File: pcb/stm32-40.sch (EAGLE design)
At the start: 103 parts, among them IC1 STM32F103RBT6, IC2 CAT24M01WI-GT3, IC3 MAX487-S, IC4 AMIS30663CANG2G, Q1 32768Hz, Q2 8MHz, Q3 MMBT2222, SW1 KSS-2EG4430, SW2 KSS-2EG4430, SW3 KSS-2EG4430, SW4 KSS-2EG4430, SW5 KSS-2EG4430, X1 MCV3, X2 MCV3

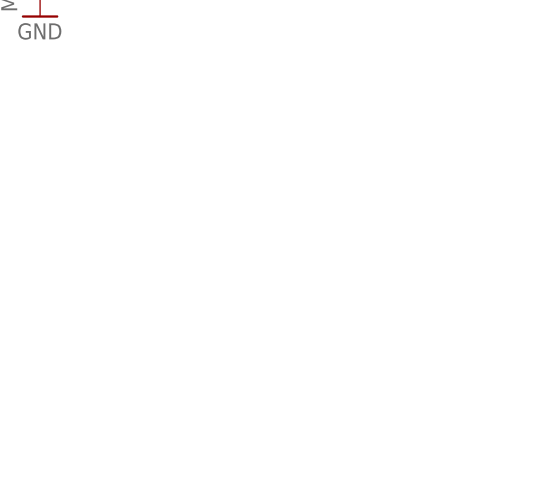
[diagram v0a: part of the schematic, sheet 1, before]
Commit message: stm32-40 ready to production PCB. some changes in platform
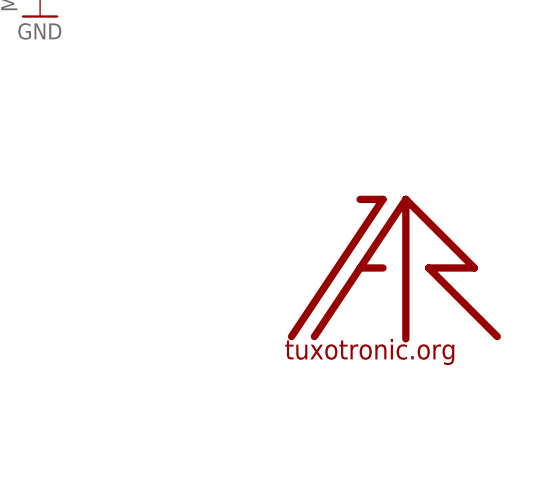
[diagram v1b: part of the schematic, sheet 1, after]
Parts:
- added U$1: LOGO, logo:LOGO
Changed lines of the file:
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@@
 <layer number="101" name="Patch_Top" color="12" fill="4" visible="yes" active="yes"/>
 <layer number="102" name="bot_pads" color="7" fill="5" visible="no" active="yes"/>
+<layer number="103" name="REF" color="7" fill="1" visible="yes" active="yes"/>
 <layer number="104" name="S_DOKU" color="7" fill="1" visible="no" active="yes"/>
 <layer number="105" name="Beschreib" color="9" fill="1" visible="no" active="no"/>
@@
 <layer number="107" name="BD-Top" color="5" fill="1" visible="no" active="no"/>
 <layer number="116" name="Patch_BOT" color="9" fill="4" visible="yes" active="yes"/>
+<layer number="121" name="_tsilk" color="7" fill="1" visible="no" active="yes"/>
+<layer number="122" name="_bsilk" color="7" fill="1" visible="no" active="yes"/>
+<layer number="125" name="_tNames" color="7" fill="1" visible="no" active="yes"/>
+<layer number="144" name="Drill_legend" color="7" fill="1" visible="no" active="yes"/>
 <layer number="151" name="HeatSink" color="7" fill="1" visible="no" active="yes"/>
 <layer number="199" name="Contour" color="7" fill="1" visible="no" active="yes"/>
 <layer number="200" name="200bmp" color="1" fill="10" visible="no" active="no"/>
 <layer number="201" name="201bmp" color="2" fill="1" visible="no" active="no"/>
+<layer number="202" name="202bmp" color="7" fill="1" visible="yes" active="yes"/>
+<layer number="203" name="203bmp" color="4" fill="10" visible="no" active="yes"/>
+<layer number="204" name="204bmp" color="5" fill="10" visible="no" active="yes"/>
+<layer number="205" name="205bmp" color="6" fill="10" visible="no" active="yes"/>
+<layer number="206" name="206bmp" color="7" fill="10" visible="no" active="yes"/>
+<layer number="207" name="207bmp" color="8" fill="10" visible="no" active="yes"/>
+<layer number="208" name="208bmp" color="9" fill="10" visible="no" active="yes"/>
+<layer number="209" name="209bmp" color="7" fill="1" visible="no" active="yes"/>
+<layer number="210" name="210bmp" color="7" fill="1" visible="no" active="yes"/>
+<layer number="211" name="211bmp" color="7" fill="1" visible="no" active="yes"/>
+<layer number="212" name="212bmp" color="7" fill="1" visible="no" active="yes"/>
+<layer number="213" name="213bmp" color="7" fill="1" visible="no" active="yes"/>
+<layer number="214" name="214bmp" color="7" fill="1" visible="no" active="yes"/>
+<layer number="215" name="215bmp" color="7" fill="1" visible="no" active="yes"/>
+<layer number="216" name="216bmp" color="7" fill="1" visible="no" active="yes"/>
+<layer number="217" name="217bmp" color="18" fill="1" visible="no" active="no"/>
+<layer number="218" name="218bmp" color="19" fill="1" visible="no" active="no"/>
+<layer number="219" name="219bmp" color="20" fill="1" visible="no" active="no"/>
+<layer number="220" name="220bmp" color="21" fill="1" visible="no" active="no"/>
+<layer number="221" name="221bmp" color="22" fill="1" visible="no" active="no"/>
+<layer number="222" name="222bmp" color="23" fill="1" visible="no" active="no"/>
+<layer number="223" name="223bmp" color="24" fill="1" visible="no" active="no"/>
+<layer number="224" name="224bmp" color="25" fill="1" visible="no" active="no"/>
 <layer number="231" name="Eagle3D_PG1" color="7" fill="1" visible="yes" active="yes"/>
 <layer number="232" name="Eagle3D_PG2" color="7" fill="1" visible="yes" active="yes"/>
@@
 <part name="L1" library="rc-master-smd" deviceset="FB_" device="0603" value="bead"/>
 <part name="+3V2" library="supply1" deviceset="+3V3" device=""/>
-<part name="FRAME1" library="frames-tt.org" deviceset="A3L-LOC" device=""/>
+<part name="FRAME1" library="frames-tt.org" deviceset="A3L-LOC" device="" value="MCU"/>
 <part name="IC2" library="stm32-by-pb" deviceset="AT24C*" device="S" technology="256" value="CAT24M01WI-GT3"/>
 <part name="C12" library="rc-master-smd" deviceset="C_" device="0603" value="0.1"/>
@@
 <part name="R9" library="rc-master-smd" deviceset="R_" device="0603" value="10K"/>
 <part name="R10" library="rc-master-smd" deviceset="R_" device="0603" value="10K"/>
-<part name="FRAME2" library="frames-tt.org" deviceset="A3L-LOC" device=""/>
+<part name="FRAME2" library="frames-tt.org" deviceset="A3L-LOC" device="" value="Connections"/>
 <part name="IC4" library="interfaces" deviceset="SN65HVD230" device="" value="AMIS30663CANG2G"/>
 <part name="+3V19" library="supply1" deviceset="+3V3" device=""/>
@@
 <part name="R50" library="rc-master-smd" deviceset="R_" device="0603" value="1K"/>
 <part name="GND13" library="supply1" deviceset="GND" device=""/>
+<part name="U$1" library="logo" deviceset="LOGO" device=""/>
 </parts>
 <sheets>
@@
 <instance part="R50" gate="G$1" x="177.8" y="38.1" rot="R90"/>
 <instance part="GND13" gate="1" x="177.8" y="30.48"/>
+<instance part="U$1" gate="G$1" x="355.6" y="25.4"/>
 </instances>
 <busses>

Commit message: little button fix
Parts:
- added R51: 330, rc-master-smd:R_0603
- C1, C2: value 10pF -> 0.1
- C14, C16: value 100uF/6V3 -> 0.1; device rc-master-smd:CP_SMCD -> rc-master-smd:C_0603
- C17: device rc-master-smd:C_0805 -> rc-master-smd:C_0603
- C19, C20: value 0.1 -> 560pF
- C21: value 0.1 -> 100uF/6V3; device rc-master-smd:C_0603 -> rc-master-smd:CP_SMCD
- C22: value 560pF -> 0.1; device rc-master-smd:C_0603 -> rc-master-smd:C_0805
- C23: value 560pF -> 100uF/6V3; device rc-master-smd:C_0603 -> rc-master-smd:CP_SMCD
- C3: value 22pF -> 0.1
- C4: value 22pF -> 10pF
- C5: value 0.1 -> 10pF
- C6, C7: value 0.1 -> 22pF
- IC1: value STM32F103RBT6 -> CAT24M01WI-GT3; device stm32:STM32F103R -> stm32-by-pb:AT24C256S
- IC2: value CAT24M01WI-GT3 -> STM32F103RBT6; device stm32-by-pb:AT24C256S -> stm32:STM32F103R
- IC3: value MAX487-S -> AMIS30663CANG2G; device rs232-rs485:MAX487-S -> interfaces:SN65HVD230
- IC4: value AMIS30663CANG2G -> MAX487-S; device interfaces:SN65HVD230 -> rs232-rs485:MAX487-S
- R1, R2: value 220 -> 10K
- R10: value 10K -> 2.2K
- R11, R41: value 4.7K -> 10K
- R12: value 4.7K -> 1K
- R13, R22: value 10 -> 2K
- R14: value 10 -> 3.9K
- R15: value 10 -> 1M
- R16: value 10 -> 1K
- R17, R18, R19: value 10 -> 200
- R20: value 10 -> 4.7K
- R23: value 10 -> 10K
- R24: value 10 -> 100
- R25, R27: value 560 -> 10
- R26: value 10K -> 10
- R28, R30: value 120 -> 10; device rc-master-smd:R_0805 -> rc-master-smd:R_0603
- R29, R31: value 330 -> 10
- R3, R4: value 10K -> 4.7K
- R32: value 0 -> 10
- R33, R34, R35: value 100 -> 10
- R36: value NC -> 10
- R42: value 200 -> 0
- R43: value 10 -> NC
- R44: value 2K -> 560
- R45: value 200 -> 100
- R46: value 200 -> 560
- R47: value 1K -> 100
- R48: value 2K -> 120; device rc-master-smd:R_0603 -> rc-master-smd:R_0805
- R49: value 3.9K -> 120; device rc-master-smd:R_0603 -> rc-master-smd:R_0805
- R5: value 10K -> 220
- R50: value 1K -> 330
- R6: value 2.2K -> 220
- R7: value 1M -> 10K
- renumbered JP2 to JP1, STMP40 to STMP1
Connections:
- new net PB5: IC2.PB5/I2C1_SMBA/(TIM3_CH2/SPI1_MOSI), R7.1
- net !LCD_CS: now also R19.2, R20.1; no longer R41.1, R46.2
- net !RESET: now also C3.1, IC2.!RESET, R11.1, SW1.S; no longer C5.1, IC1.!RESET, R8.1, SW2.S
- net +3V3: now also C1.1, C17.1, C2.1, C22.1, C23.+, IC1.VCC, IC2.VDD@1, IC2.VDD@2, IC2.VDD@3, IC2.VDD@4, R1.2, R2.2, R20.2, R21.2, R23.2, R3.2, R4.2, R42.1, R5.1, SW2.S; no longer C11.1, C15.1, C16.+, C20.1, C7.1, IC1.VDD@1, IC1.VDD@2, IC1.VDD@3, IC1.VDD@4, IC2.VCC, R1.1, R10.2, R12.2, R32.1, R41.2, R43.2, R5.2, R8.2, R9.2, SW1.S
- net +5V: now also C14.1, C15.1, C16.1, C21.+, IC3.VDD, IC4G$2.VCC, R46.2; no longer C14.+, C17.1, C18.1, C19.1, IC3G$2.VCC, IC4.VDD, R25.2
- net BOOT0: now also IC2.BOOT0, R8.1; no longer IC1.BOOT0, IC1.PB5/I2C1_SMBA/(TIM3_CH2/SPI1_MOSI), R4.1
- net BOOT1: now also IC2.PB2/BOOT1, R6.1, R9.1; no longer IC1.PB2/BOOT1, R2.1, R3.1
- net CAN_CTRL: now also IC3.RS, R42.2, R43.2; no longer IC4.RS, R32.2, R36.2
- net CAN_H: now also R49.1; no longer R30.1
- net CAN_RX: now also IC2.PA11/CANRX/USBDM/USART1_CTS/TIM1_CH4, R24.1; no longer IC1.PA11/CANRX/USBDM/USART1_CTS/TIM1_CH4, R33.1
- net CAN_TX: now also IC2.PA12/CANTX/USBDP/USART1_RTS/TIM1_ETR, IC3.TXD; no longer IC1.PA12/CANTX/USBDP/USART1_RTS/TIM1_ETR, IC4.TXD
- net DE3: now also IC2.PC12/(USART3_CK), IC4G$1.DI; no longer IC1.PC12/(USART3_CK), IC3G$1.DI
- net GND: now also C14.2, C16.2, C21.-, C23.-, IC1.A0, IC1.A1, IC1.A2, IC1.GND, IC1.WP, IC2.VSS@1, IC2.VSS@2, IC2.VSS@3, IC2.VSS@4, IC2.VSSA, IC3.VSS, IC4G$2.GND, R10.1, R16.1, R41.1, R43.1, R44.1, R9.2, SW1.P; no longer C14.-, C16.-, C21.2, C23.2, IC1.VSS@1, IC1.VSS@2, IC1.VSS@3, IC1.VSS@4, IC1.VSSA, IC2.A0, IC2.A1, IC2.A2, IC2.GND, IC2.WP, IC3G$2.GND, IC4.VSS, R26.1, R27.1, R3.2, R36.1, R50.1, R6.1, SW2.P
- net LCD_CLK: now also R18.2; no longer R45.2
- net LCD_DATA: now also R17.2; no longer R42.2
- net N$1: now also C18.1, IC3.VREF; no longer C21.1, IC4.VREF
- net N$10: now also R51.1; no longer R31.1
- net N$11: now also R33.1; no longer R21.1
- net N$13: now also R5.2; no longer R1.2
- net N$14: now also R34.1; no longer R22.1
- net N$15: now also R25.1; no longer R13.1
- net N$16: now also R26.1; no longer R14.1
- net N$17: now also R27.1; no longer R15.1
- net N$18: now also R28.1; no longer R16.1
- net N$19: now also R29.1; no longer R17.1
- net N$2: now also R49.2; no longer R30.2
- net N$20: now also R30.1; no longer R18.1
- net N$21: now also R31.1; no longer R19.1
- net N$22: now also R32.1; no longer R20.1
- net N$23: now also R35.1; no longer R23.1
- net N$24: now also R36.1; no longer R24.1
- net N$3: now also R10.2, R7.2, R8.2, SW2.P; no longer R4.2, R6.2, SW1.P
- net N$30: now also R6.2; no longer R2.2
- net N$31: now also R21.1; no longer R43.1
- net N$32: now also R22.1; no longer R44.1
- net N$33: now also R12.1; no longer R47.1
- net N$34: now also R13.1; no longer R48.1
- net N$35: now also R14.1; no longer R49.1
- net N$44: now also IC4G$1.A, R46.1; no longer IC3G$1.A, R25.1
- net N$51: now also IC3.CANH, R45.2; no longer IC4.CANH, R34.2
- net N$52: now also IC3.CANL, R47.2; no longer IC4.CANL, R35.2
- net N$54: now also C20.1, R47.1; no longer C23.1, R35.1
- net N$55: now also C19.1, R45.1; no longer C22.1, R34.1
- net N$6: now also IC4G$1.B, R44.2; no longer IC3G$1.B, R27.2
- net N$7: now also IC3.RXD, R24.2; no longer IC4.RXD, R33.2
- net N$8: now also R48.2; no longer R28.2
- net N$9: now also R50.1; no longer R29.1
- net OSC32_IN: now also C4.1, IC2.PC14/OSC32_IN; no longer C1.1, IC1.PC14/OSC32_IN
- net OSC32_OUT: now also C5.1, IC2.PC15/OSC32_OUT; no longer C2.1, IC1.PC15/OSC32_OUT
- net OSC_IN: now also C6.1, IC2.OSC_IN/(PD0/CANRX), R15.2; no longer C3.1, IC1.OSC_IN/(PD0/CANRX), R7.2
- net OSC_OUT: now also C7.1, IC2.OSC_OUT/(PD1/CANTX), R15.1; no longer C4.1, IC1.OSC_OUT/(PD1/CANTX), R7.1
- net PA0: now also IC2.PA0/WKUP/USART2_CTS/ADC12_IN0/TIM2_CH1_ETR, R12.2, R13.2, R14.2, R16.2; no longer IC1.PA0/WKUP/USART2_CTS/ADC12_IN0/TIM2_CH1_ETR, R47.2, R48.2, R49.2, R50.2
- net PA1: now also IC2.PA1/USART2_RTS/ADC12_IN1/TIM2_CH2, R19.1; no longer IC1.PA1/USART2_RTS/ADC12_IN1/TIM2_CH2, R46.1
- net PA15: now also IC2.JTDI/(TIM2_CH1_ETR/PA15/SPI1_NSS); no longer IC1.JTDI/(TIM2_CH1_ETR/PA15/SPI1_NSS)
- net PA2: now also IC2.PA2/USART2_TX/ADC12_IN2/TIM2_CH3, R17.1; no longer IC1.PA2/USART2_TX/ADC12_IN2/TIM2_CH3, R42.1
- net PA3: now also IC2.PA3/USART2_RX/ADC12_IN3/TIM2_CH4; no longer IC1.PA3/USART2_RX/ADC12_IN3/TIM2_CH4
- net PA4: now also IC2.PA4/SPI1_NSS/ADC12_IN4/USART2_CK, R18.1; no longer IC1.PA4/SPI1_NSS/ADC12_IN4/USART2_CK, R45.1
- net PA5: now also IC2.PA5/SPI1_SCK/ADC12_IN5; no longer IC1.PA5/SPI1_SCK/ADC12_IN5
- net PA6: now also IC2.PA6/SPI1_MISO/ADC12_IN6/TIM3_CH1; no longer IC1.PA6/SPI1_MISO/ADC12_IN6/TIM3_CH1
- net PA7: now also IC2.PA7SPI1_MOSI/ADC12_IN7/TIM3_CH2; no longer IC1.PA7SPI1_MOSI/ADC12_IN7/TIM3_CH2
- net PA8: now also IC2.PA8/USART1_CK/MCO/TIM1_CH1; no longer IC1.PA8/USART1_CK/MCO/TIM1_CH1
- net PB0: now also IC2.PB0/ADC12_IN8/TIM3_CH3/(TIM1_CH2N); no longer IC1.PB0/ADC12_IN8/TIM3_CH3/(TIM1_CH2N)
- net PB1: now also IC2.PB1/ADC12_IN9/TIM3_CH4/(TIM1_CH3N); no longer IC1.PB1/ADC12_IN9/TIM3_CH4/(TIM1_CH3N)
- net PC0: now also IC2.PC0/ADC10, R33.2; no longer IC1.PC0/ADC10, R21.2
- net PC1: now also IC2.PC1/ADC11, R34.2; no longer IC1.PC1/ADC11, R22.2
- net PC13: now also IC2.PC13/TAMPER-RTC; no longer IC1.PC13/TAMPER-RTC
- net PC2: now also IC2.PC2/ADC12, R35.2; no longer IC1.PC2/ADC12, R23.2
- net PC3: now also IC2.PC3/ADC13, R36.2; no longer IC1.PC3/ADC13, R24.2
- net PC4: now also IC2.PC4/ADC14; no longer IC1.PC4/ADC14
- net PC5: now also IC2.PC5/ADC15; no longer IC1.PC5/ADC15
- net PD2: now also IC2.PD2/TIM3_ETR, R22.2; no longer IC1.PD2/TIM3_ETR, R44.2
- net RS485_A: now also R48.1; no longer R28.1
- net RXD1: now also IC2.PA10/USART1_RX/TIM1_CH3, R23.1; no longer IC1.PA10/USART1_RX/TIM1_CH3, R5.1
- net RXD3: now also IC2.PC11/(USART3_RX), IC4G$1.RO; no longer IC1.PC11/(USART3_RX), IC3G$1.RO
- net SCL2: now also IC1.SCL, IC2.PB10/I2C2_SCL/USART3_TX/(TIM2_CH3), R3.1; no longer IC1.PB10/I2C2_SCL/USART3_TX/(TIM2_CH3), IC2.SCL, R11.1
- net SDA2: now also IC1.SDA, IC2.PB11/I2C2_SDA/USART3_RX/(TIM2_CH4), R4.1; no longer IC1.PB11/I2C2_SDA/USART3_RX/(TIM2_CH4), IC2.SDA, R12.1
- net SPI2_MISO: now also IC2.PB14/SPI2_MISO/TIM1_CH2N/USART3_RTS; no longer IC1.PB14/SPI2_MISO/TIM1_CH2N/USART3_RTS
- net SPI2_MOSI: now also IC2.PB15/SPI2_MOSI/TIM1_CH3N; no longer IC1.PB15/SPI2_MOSI/TIM1_CH3N
- net SPI2_NSS: now also IC2.PB12/SPI2_NSS/I2C2_SMBAI/TIM1_BKIN/USART3_CK; no longer IC1.PB12/SPI2_NSS/I2C2_SMBAI/TIM1_BKIN/USART3_CK
- net SPI2_SCLK: now also IC2.PB13/SPI2_SCK/TIM1_CH1N/USART3_CTS; no longer IC1.PB13/SPI2_SCK/TIM1_CH1N/USART3_CTS
- net SW3: now also IC2.JTDO/(TIM2_CH2/PB3/TRACESWO/SPI1_SCK), R50.2; no longer IC1.JTDO/(TIM2_CH2/PB3/TRACESWO/SPI1_SCK), R29.2
- net SW4: now also IC2.JTNRST/(PB4/TIM3_CH1/SPI1_MISO), R51.2; no longer IC1.JTNRST/(PB4/TIM3_CH1/SPI1_MISO), R31.2
- net SWCLK: now also IC2.JTCK-SWCLK/(PA14), R1.1; no longer IC1.JTCK-SWCLK/(PA14), R9.1
- net SWDIO: now also IC2.JTMS-SWDIO/(PA13), R2.1; no longer IC1.JTMS-SWDIO/(PA13), R10.1
- net TIM3_CH1: now also IC2.PC6/(TIM3_CH1), R25.2; no longer IC1.PC6/(TIM3_CH1), R13.2
- net TIM3_CH2: now also IC2.PC7/(TIM3_CH2), R26.2; no longer IC1.PC7/(TIM3_CH2), R14.2
- net TIM3_CH3: now also IC2.PC8/(TIM3_CH3), R27.2; no longer IC1.PC8/(TIM3_CH3), R15.2
- net TIM3_CH4: now also IC2.PC9/(TIM3_CH4), R28.2; no longer IC1.PC9/(TIM3_CH4), R16.2
- net TIM4_CH1: now also IC2.PB6/I2C1_SCL/TIM4_CH1/(USART1_TX), R29.2; no longer IC1.PB6/I2C1_SCL/TIM4_CH1/(USART1_TX), R17.2
- net TIM4_CH2: now also IC2.PB7/I2C1_SDA/TIM4_CH2/(USART1_RX), R30.2; no longer IC1.PB7/I2C1_SDA/TIM4_CH2/(USART1_RX), R18.2
- net TIM4_CH3: now also IC2.PB8/TIM4_CH3/(I2C1_SCL/CANRX), R31.2; no longer IC1.PB8/TIM4_CH3/(I2C1_SCL/CANRX), R19.2
- net TIM4_CH4: now also IC2.PB9/TIM4_CH4/(I2C1_SDA/CANTX), R32.2; no longer IC1.PB9/TIM4_CH4/(I2C1_SDA/CANTX), R20.2
- net TXD1: now also IC2.PA9/USART1_TX/TIM1_CH2; no longer IC1.PA9/USART1_TX/TIM1_CH2
- net TXD3: now also IC2.PC10/(USART3_TX), IC4G$1.DE, IC4G$1.RE/, R41.2; no longer IC1.PC10/(USART3_TX), IC3G$1.DE, IC3G$1.RE/, R26.2
- net VBAT: now also IC2.VBAT; no longer IC1.VBAT
- net VDDA: now also C11.1, IC2.VDDA; no longer C6.1, IC1.VDDA
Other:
- moved on the sheet: C1, C11, C12, C15, C17, C18, C19, C2, C20, C22, C3, C4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
